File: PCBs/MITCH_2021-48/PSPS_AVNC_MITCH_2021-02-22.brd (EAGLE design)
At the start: 25.4 x 50.8 mm, 54 parts, among them J1 A-1JB, U0-C STM32F411CEUX, U1-S ICM-20948, U11-S SN74LV1T34, U12-S SN74LV1T34, U13-S SN74LV1T34, U14-S SN74LV1T34, U14-S1 SN74LV1T34, U14-S2 SN74LV1T34, U2-S MMA1211KEG

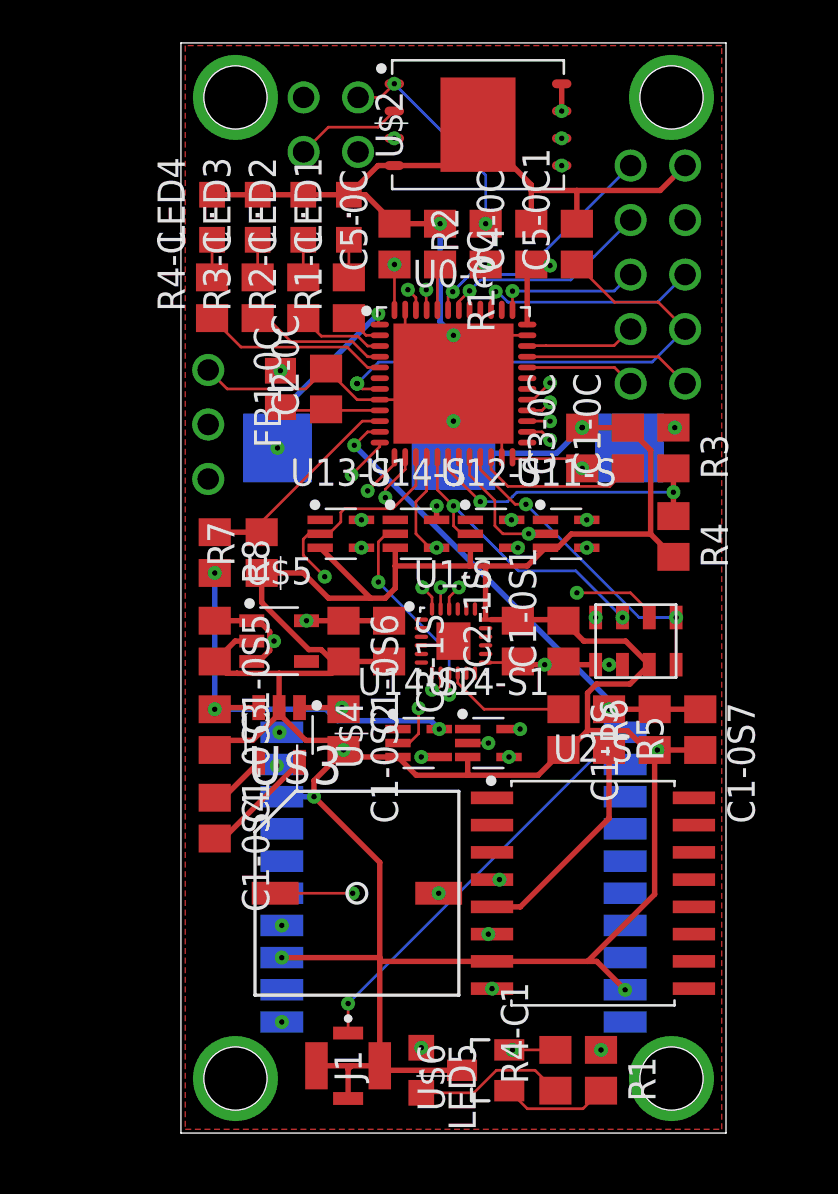
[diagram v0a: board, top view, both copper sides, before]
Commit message: Updated silk screen
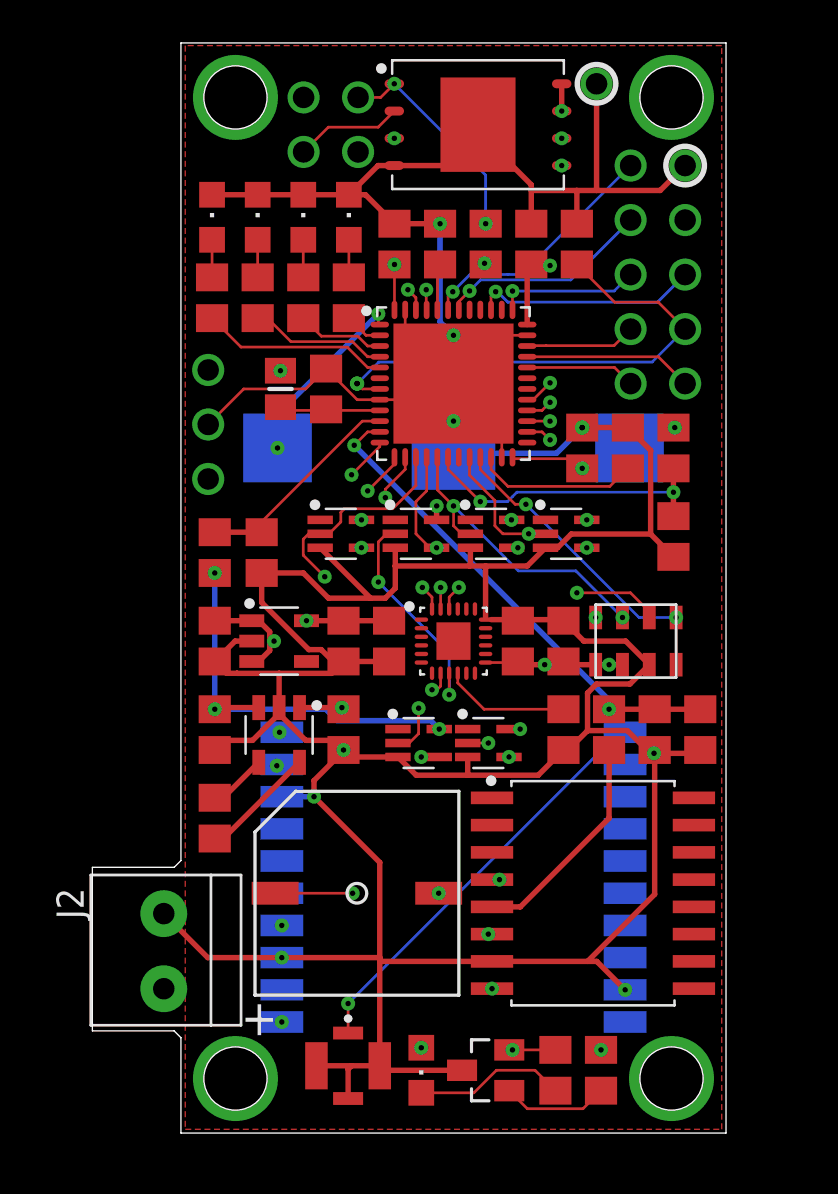
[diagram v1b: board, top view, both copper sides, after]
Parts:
- added J2: 1X2-3.5MM, adafruit:1X2-3.5MM
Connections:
- net 3V3: now also J2.2
- net GND: now also J2.1
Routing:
- net GND: track 238.5 -> 250.0 mm, vias 12 -> 13
- net 3V3: track 135.7 -> 141.9 mm
- net NRST: track 31.6 -> 31.0 mm
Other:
- board size 25.4 x 50.8 mm -> 29.5 x 50.8 mm
- board text added: "+"
- board text added: "+3.3V"
- board text added: "+X"
- board text added: "+Y"
- board text added: "+Z"
- board text added: "ACCEL & GYRO"
- board text added: "GND"
- board text added: "MAG"
- board text added: "MITCH 2021 1.0"
- board text added: "Purdue Space Program Solids"

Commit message: Final tweaks for MITCH 2021.0
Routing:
- net SPI2_MISO: track 24.7 -> 24.2 mm
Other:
- board text added: "MITCH 2021.0"
- board text removed: "MITCH 2021 1.0"
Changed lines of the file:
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@@
 <setting verticaltext="up"/>
 </settings>
-<grid distance="0.25" unitdist="mm" unit="mm" style="lines" multiple="1" display="yes" altdistance="12.5" altunitdist="mil" altunit="mil"/>
+<grid distance="0.125" unitdist="mm" unit="mm" style="lines" multiple="1" display="yes" altdistance="0.0625" altunitdist="mm" altunit="mm"/>
 <layers>
 <layer number="1" name="Top" color="4" fill="1" visible="yes" active="yes"/>
@@
 <hole x="10.16" y="13.335" drill="2.9464"/>
 <hole x="-10.16" y="13.335" drill="2.9464"/>
-<text x="0" y="-33.02" size="1.4224" layer="26" rot="SMR0" align="center">MITCH 2021 1.0</text>
+<text x="0" y="-33.02" size="1.4224" layer="26" rot="SMR0" align="center">MITCH 2021.0</text>
 <wire x1="-12.7" y1="-34.925" x2="-12.7" y2="-30.48" width="0" layer="20"/>
 <wire x1="-12.7" y1="-30.48" x2="-13.0175" y2="-30.1625" width="0" layer="20"/>
@@
 <circle x="6.6675" y="13.97" radius="0.898025" width="0.254" layer="21"/>
 <circle x="6.6675" y="13.97" radius="0.898025" width="0.254" layer="22"/>
+<circle x="-11.43" y="-1.905" radius="0.898025" width="0.254" layer="22"/>
+<circle x="-11.43" y="-1.905" radius="0.898025" width="0.254" layer="21"/>
+<wire x1="5.3975" y1="3.4925" x2="5.3975" y2="2.54" width="0.3048" layer="25"/>
+<wire x1="5.3975" y1="2.54" x2="5.3975" y2="1.905" width="0.3048" layer="25"/>
+<wire x1="5.3975" y1="1.905" x2="5.08" y2="1.5875" width="0.3048" layer="25"/>
+<wire x1="5.08" y1="1.5875" x2="4.7625" y2="1.5875" width="0.3048" layer="25"/>
+<wire x1="4.7625" y1="1.5875" x2="4.445" y2="1.905" width="0.3048" layer="25"/>
+<wire x1="5.3975" y1="2.54" x2="5.715" y2="2.54" width="0.3048" layer="25"/>
+<wire x1="5.715" y1="2.54" x2="6.6675" y2="3.4925" width="0.3048" layer="25"/>
+<wire x1="5.715" y1="2.54" x2="6.6675" y2="1.5875" width="0.3048" layer="25"/>
+<wire x1="8.8525" y1="-5.7575" x2="8.8525" y2="-6.71" width="0.3048" layer="26"/>
+<wire x1="8.8525" y1="-6.71" x2="8.8525" y2="-7.345" width="0.3048" layer="26"/>
+<wire x1="8.8525" y1="-7.345" x2="9.17" y2="-7.6625" width="0.3048" layer="26"/>
+<wire x1="9.17" y1="-7.6625" x2="9.4875" y2="-7.6625" width="0.3048" layer="26"/>
+<wire x1="9.4875" y1="-7.6625" x2="9.805" y2="-7.345" width="0.3048" layer="26"/>
+<wire x1="8.8525" y1="-6.71" x2="8.535" y2="-6.71" width="0.3048" layer="26"/>
+<wire x1="8.535" y1="-6.71" x2="7.5825" y2="-5.7575" width="0.3048" layer="26"/>
+<wire x1="8.535" y1="-6.71" x2="7.5825" y2="-7.6625" width="0.3048" layer="26"/>
+<wire x1="-4.25" y1="4" x2="-5.5" y2="4" width="0.254" layer="25"/>
+<wire x1="-6.375" y1="4" x2="-7.625" y2="4" width="0.254" layer="25"/>
+<wire x1="-8.5" y1="4" x2="-9.75" y2="4" width="0.254" layer="25"/>
+<wire x1="-10.625" y1="4" x2="-11.875" y2="4" width="0.254" layer="25"/>
+<wire x1="-2.125" y1="6.5" x2="-3.375" y2="6.5" width="0.254" layer="25"/>
+<wire x1="0" y1="6.5" x2="-1.25" y2="6.5" width="0.254" layer="25"/>
+<wire x1="2.125" y1="6.5" x2="0.875" y2="6.5" width="0.254" layer="25"/>
+<wire x1="4.25" y1="6.5" x2="3" y2="6.5" width="0.254" layer="25"/>
+<wire x1="6.375" y1="6.5" x2="5.125" y2="6.5" width="0.254" layer="25"/>
+<wire x1="6.625" y1="-3" x2="5.375" y2="-3" width="0.254" layer="25"/>
+<wire x1="8.75" y1="-3" x2="7.5" y2="-3" width="0.254" layer="25"/>
+<wire x1="10.875" y1="-3" x2="9.625" y2="-3" width="0.254" layer="25"/>
+<wire x1="10.875" y1="-7.125" x2="9.625" y2="-7.125" width="0.254" layer="25"/>
+<wire x1="5.75" y1="-12" x2="4.5" y2="-12" width="0.254" layer="25"/>
+<wire x1="3.625" y1="-12" x2="2.375" y2="-12" width="0.254" layer="25"/>
+<wire x1="-8.3125" y1="-7.875" x2="-9.5625" y2="-7.875" width="0.254" layer="25"/>
+<wire x1="-10.5" y1="-7.875" x2="-11.75" y2="-7.875" width="0.254" layer="25"/>
+<wire x1="-5.3125" y1="-0.25" x2="-6.5625" y2="-0.25" width="0.254" layer="25"/>
+<wire x1="-10.5" y1="-12" x2="-11.75" y2="-12" width="0.254" layer="25"/>
+<wire x1="-4.5" y1="-12" x2="-5.75" y2="-12" width="0.254" layer="25"/>
+<wire x1="-2.375" y1="-12" x2="-3.625" y2="-12" width="0.254" layer="25"/>
+<wire x1="-10.5" y1="-16.125" x2="-11.75" y2="-16.125" width="0.254" layer="25"/>
+<wire x1="-4.5" y1="-16.125" x2="-5.75" y2="-16.125" width="0.254" layer="25"/>
+<wire x1="5.75" y1="-16.125" x2="4.5" y2="-16.125" width="0.254" layer="25"/>
+<wire x1="7.875" y1="-16.125" x2="6.625" y2="-16.125" width="0.254" layer="25"/>
+<wire x1="10" y1="-16.125" x2="8.75" y2="-16.125" width="0.254" layer="25"/>
+<wire x1="12.125" y1="-16.125" x2="10.875" y2="-16.125" width="0.254" layer="25"/>
+<wire x1="-10.5" y1="-20.25" x2="-11.75" y2="-20.25" width="0.254" layer="25"/>
+<wire x1="5.375" y1="-32" x2="4.125" y2="-32" width="0.254" layer="25"/>
+<wire x1="7.5" y1="-32" x2="6.25" y2="-32" width="0.254" layer="25"/>
 </plain>
 <attributes>
@@
 <attribute name="VALUE" x="8.29" y="5.23" size="1.27" layer="27" rot="R90"/>
 </element>
-<element name="J2" library="adafruit" library_urn="urn:adsk.eagle:library:420" package="1X2-3.5MM" package3d_urn="urn:adsk.eagle:package:6240635/1" value="1X2-3.5MM" x="-13.5" y="-26.5" smashed="yes" rot="R90">
-<attribute name="NAME" x="-18.5" y="-23.5" size="1.27" layer="25" rot="R270"/>
-</element>
+<element name="J2" library="adafruit" library_urn="urn:adsk.eagle:library:420" package="1X2-3.5MM" package3d_urn="urn:adsk.eagle:package:6240635/1" value="1X2-3.5MM" x="-13.5" y="-26.5" smashed="yes" rot="R90"/>
 </elements>
 <signals>
@@
 <wire x1="5.5623" y1="10.9113" x2="5.5623" y2="-1.5627" width="0.127" layer="2"/>
 <wire x1="5.5623" y1="-1.5627" x2="4.5" y2="-2.625" width="0.127" layer="2"/>
-<wire x1="-1.77404375" y1="11.43" x2="5.0436" y2="11.43" width="0.127" layer="2"/>
-<wire x1="-2.29274375" y1="11.9487" x2="-1.77404375" y2="11.43" width="0.127" layer="2"/>
-<wire x1="-5.5987" y1="11.9487" x2="-2.29274375" y2="11.9487" width="0.127" layer="2"/>
+<wire x1="-2.02404375" y1="11.43" x2="5.0436" y2="11.43" width="0.127" layer="2"/>
+<wire x1="-2.54274375" y1="11.9487" x2="-2.02404375" y2="11.43" width="0.127" layer="2"/>
+<wire x1="-5.5987" y1="11.9487" x2="-2.54274375" y2="11.9487" width="0.127" layer="2"/>
 <wire x1="-5.5987" y1="11.9487" x2="-6.95" y2="13.3" width="0.127" layer="2"/>
 <wire x1="-6.95" y1="13.3" x2="-6.985" y2="13.335" width="0.254" layer="2"/>
@@
 <wire x1="-5.8313" y1="11.9487" x2="-3.5089" y2="11.9487" width="0.127" layer="1"/>
 <wire x1="-2.7576" y1="12.7" x2="-3.5089" y2="11.9487" width="0.127" layer="1"/>
-<wire x1="4.5" y1="-1.75" x2="3" y2="-1.75" width="0.127" layer="2"/>
-<wire x1="-0.625" y1="5.185" x2="-6.235" y2="10.795" width="0.127" layer="2"/>
-<wire x1="-6.985" y1="10.795" x2="-6.235" y2="10.795" width="0.127" layer="2"/>
-<wire x1="3" y1="-1.75" x2="-0.625" y2="1.875" width="0.127" layer="2"/>
-<wire x1="-0.625" y1="1.875" x2="-0.625" y2="5.185" width="0.127" layer="2"/>
+<wire x1="4.5" y1="-1.75" x2="3.25" y2="-1.75" width="0.127" layer="2"/>
+<wire x1="-0.625" y1="4.56" x2="-6.86" y2="10.795" width="0.127" layer="2"/>
+<wire x1="-6.86" y1="10.795" x2="-6.985" y2="10.795" width="0.127" layer="2"/>
+<wire x1="3.25" y1="-1.75" x2="-0.625" y2="2.125" width="0.127" layer="2"/>
+<wire x1="-0.625" y1="2.125" x2="-0.625" y2="4.56" width="0.127" layer="2"/>
 </signal>
 <signal name="SPI2_MOSI">
@@
 <via x="10.795" y="7.62" extent="1-16" drill="1"/>
 <polygon width="0.127" layer="15">
-<vertex x="-12.5" y="15.75"/>
+<vertex x="-12.625" y="15.75"/>
+<vertex x="-12.625" y="-22.375"/>
+<vertex x="-13" y="-22.75"/>
+<vertex x="-16.625" y="-22.75"/>
+<vertex x="-16.625" y="-30"/>
+<vertex x="-13" y="-30"/>
+<vertex x="-12.5" y="-30.5"/>
 <vertex x="-12.5" y="-34.75"/>
 <vertex x="12.5" y="-34.75"/>
@@
 <polygon width="0.127" layer="1" thermals="no">
 <vertex x="-12.5" y="15.75"/>
+<vertex x="-12.5" y="-22.25"/>
+<vertex x="-13" y="-22.75"/>
+<vertex x="-16.625" y="-22.75"/>
+<vertex x="-16.625" y="-30"/>
+<vertex x="-13" y="-30"/>
+<vertex x="-12.5" y="-30.5"/>
 <vertex x="-12.5" y="-34.75"/>
 <vertex x="12.5" y="-34.75"/>
@@
 <wire x1="-1.75" y1="4" x2="-2.125" y2="4.375" width="0.127" layer="1"/>
 <via x="-2.125" y="4.375" extent="1-16" drill="0.25"/>
-<wire x1="-2.125" y1="4.375" x2="-2.125" y2="-4.75" width="0.127" layer="2"/>
 <contactref element="U14-S2" pad="2"/>
 <wire x1="-2.0873" y1="-16.75" x2="-2.5873" y2="-16.75" width="0.127" layer="1"/>
-<wire x1="-2.125" y1="-4.75" x2="-2.3125" y2="-4.9375" width="0.127" layer="2"/>
 <wire x1="-2.5873" y1="-16.75" x2="-2.0625" y2="-16.75" width="0.127" layer="1"/>
 <wire x1="-2.0625" y1="-16.75" x2="-1.625" y2="-16.3125" width="0.127" layer="1"/>
@@
 <via x="-1.625" y="-15.125" extent="1-16" drill="0.25"/>
 <wire x1="-2.3125" y1="-14.4375" x2="-1.625" y2="-15.125" width="0.127" layer="2"/>
-<wire x1="-2.3125" y1="-4.9375" x2="-2.3125" y2="-14.4375" width="0.127" layer="2"/>
+<wire x1="-2.125" y1="4.375" x2="-2.3125" y2="4.1875" width="0.127" layer="2"/>
+<wire x1="-2.3125" y1="4.1875" x2="-2.3125" y2="-14.4375" width="0.127" layer="2"/>
 </signal>
 <signal name="ALA_STATUS">

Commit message: Continued refining MITCH 2021.0
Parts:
- added R9: (no value), resistor:R0805
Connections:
- net BUTTON_IN: now also R9.1
- net GND: now also R9.2
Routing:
- net BUTTON_IN: track 7.88 -> 15.2 mm, vias 1 -> 2
- net GND: track 250.0 -> 252.9 mm
- net 5V: track 34.3 -> 33.4 mm
- net 3V3: track 141.9 -> 142.2 mm, vias 15 -> 16
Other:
- board text added: "12mm coin cell can be added to help GPS acquire lock faster"
- board text added: "3V3"
- board text added: "Apply insulation to shaded area"
- board text added: "B Elshimy"
- board text added: "B Wodetzki"
- board text added: "BATT_MEAS"
- board text added: "BUTTON"
- board text added: "BUZZER"
- board text added: "CS"
- board text added: "J Kaji"
- board text added: "J Wiley"
- board text added: "M Batistich"
- board text added: "M Paral"
- board text added: "MISO"
- board text added: "MOSI"
- board text added: "NRST"
- board text added: "R Horvath"
- board text added: "SCK"
- board text added: "SCL"
- board text added: "SDA"
- board text added: "SWCLK"
- board text added: "SWDIO"
- board text added: "SWO"
- board text added: "V Vijay"
- board text added: "WARNING: BATT_MEAS cannot exceed 3.3V Use an external voltage divider to protect the ADC. Failing to do so may destroy this device."
